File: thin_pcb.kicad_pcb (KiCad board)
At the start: 2 copper layers, 95.2 x 95.2 mm, 185 parts, among them J01 Conn_01x02, J02 Conn_01x02, J04 Conn_01x02, J06 Conn_01x02, J07 Conn_01x02, J08 Conn_01x02, J1 USB_B_Micro, J11 Conn_01x03, J12 Conn_01x03, J13 Conn_01x03, J14 Conn_01x03, J15 Conn_01x03, J16 Conn_01x03, J17 Conn_01x03, J18 Conn_01x03, J2 AudioJack4_Ground, J21 Conn_01x07, J22 Conn_01x07, J23 Conn_01x07, J24 Conn_01x07, J25 Conn_01x07, J26 Conn_01x07, J27 Conn_01x07, J28 Conn_01x07, J3 AudioJack4_Ground, J31 Conn_01x07, J32 Conn_01x07, J33 Conn_01x07, J34 Conn_01x07, J35 Conn_01x07, J36 Conn_01x07, J37 Conn_01x07, J38 Conn_01x07, J4 Conn_01x06, J41 Conn_01x04, J42 Conn_01x04, J43 Conn_01x04, J44 Conn_01x04, J45 Conn_01x04, J46 Conn_01x04, J47 Conn_01x04, J48 Conn_01x04, J5 Conn_01x06, J51 Conn_01x01, J52 Conn_01x01, J53 Conn_01x01, J54 Conn_01x01, J55 Conn_01x01, J56 Conn_01x01, J57 Conn_01x01, J58 Conn_01x01, J6 Conn_02x02, J7 Conn_01x02, SW11 SW_Push, SW12 SW_Push, SW13 SW_Push, SW14 SW_Push, SW15 SW_Push, SW21 SW_Push, SW22 SW_Push, SW23 SW_Push, SW24 SW_Push, SW25 SW_Push, SW252 SW_Push, SW31 SW_Push, SW32 SW_Push, SW33 SW_Push, SW34 SW_Push, SW35 SW_Push, SW41 SW_Push, SW42 SW_Push, SW422 SW_Push, SW43 SW_Push, SW44 SW_Push, SW45 SW_Push, SW452 SW_Push, SW51 SW_Push, SW52 SW_Push, SW522 SW_Push, SW53 SW_Push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

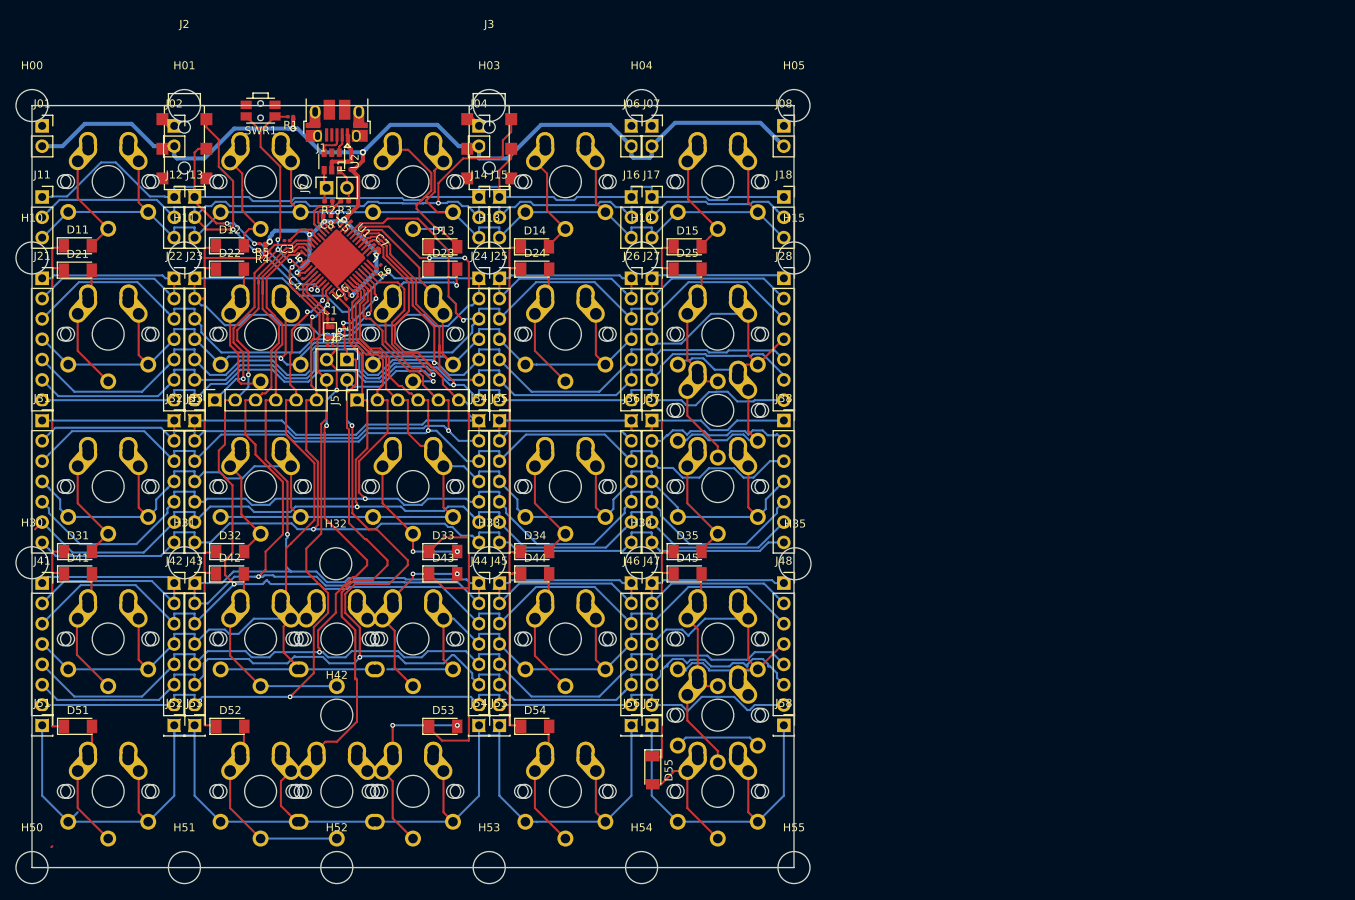
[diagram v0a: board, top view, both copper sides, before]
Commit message: hide unwanted labels
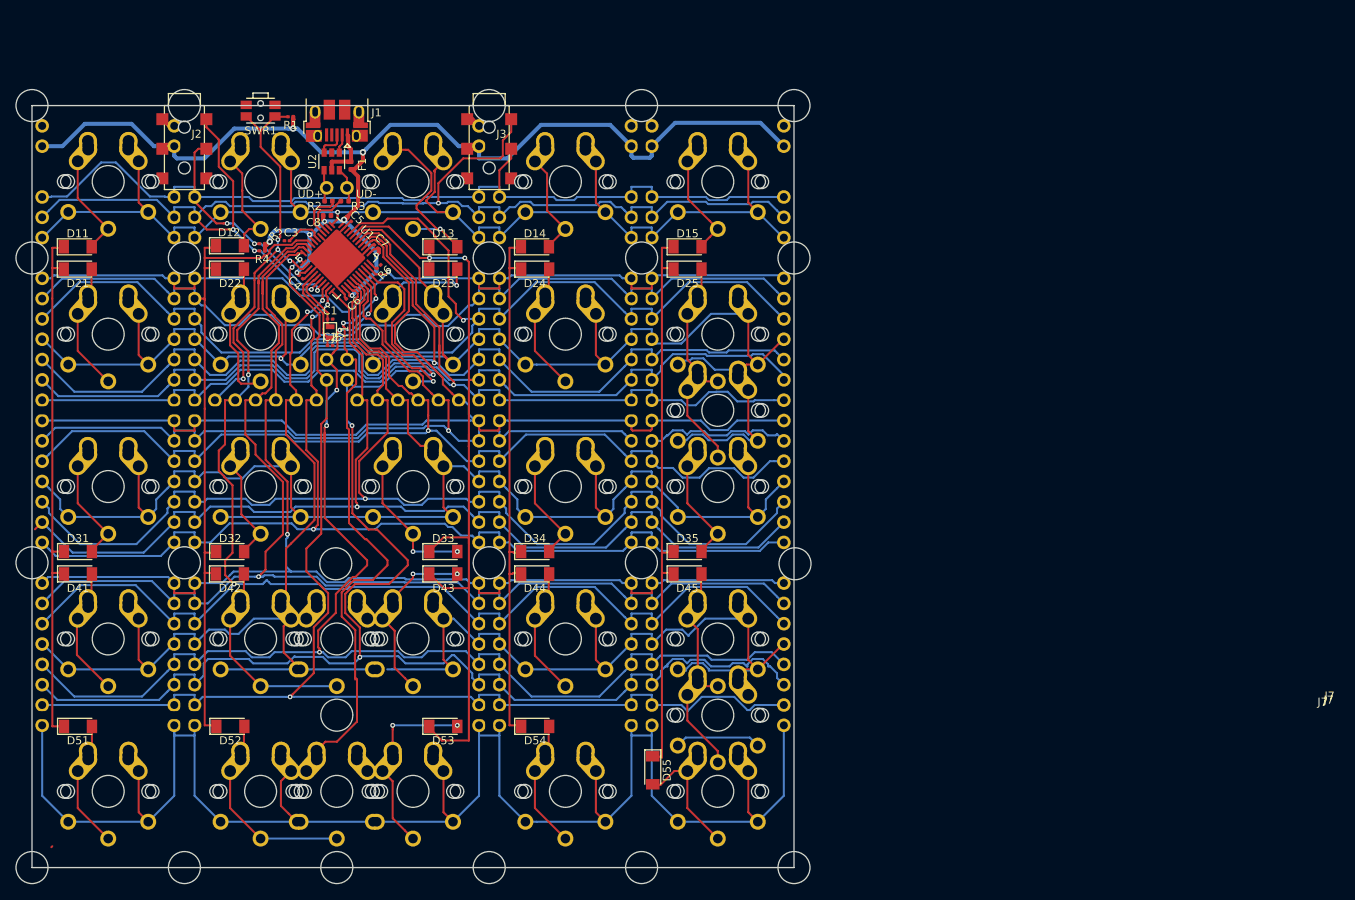
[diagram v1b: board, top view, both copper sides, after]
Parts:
- added ?: , , F.Cu at (86.7, 70.2)
- added ?: , , F.Cu at (86.0, 70.5)
- added ?: , , F.Cu at (86.9, 69.7)
- J01, J02, J04, J06, J07, J08, J7: footprint Connector_PinSocket_2.54mm:PinSocket_1x02_P2.54mm_Vertical -> lib:PinSocket_1x02_P2.54mm_Vertical
- J11, J12, J13, J14, J15, J16, J17, J18: footprint Connector_PinSocket_2.54mm:PinSocket_1x03_P2.54mm_Vertical -> lib:PinSocket_1x03_P2.54mm_Vertical
- J21, J22, J23, J24, J25, J26, J27, J28, J31, J32, J33, J34, J35, J36, J37, J38, J41, J42, J43, J44, J45, J46, J47, J48: footprint Connector_PinSocket_2.54mm:PinSocket_1x07_P2.54mm_Vertical -> lib:PinSocket_1x07_P2.54mm_Vertical
- J4, J5: footprint Connector_PinSocket_2.54mm:PinSocket_1x06_P2.54mm_Vertical -> lib:PinSocket_1x06_P2.54mm_Vertical
- J51, J52, J53, J54, J55, J56, J57, J58: footprint Connector_PinSocket_2.54mm:PinSocket_1x01_P2.54mm_Vertical -> lib:PinSocket_1x01_P2.54mm_Vertical
- J6: footprint Connector_PinSocket_2.54mm:PinSocket_2x02_P2.54mm_Vertical -> lib:PinSocket_2x02_P2.54mm_Vertical
- moved D21 0.13 mm to (57.1, 79.5)
- moved D11 0.13 mm to (57.1, 76.7)
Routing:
- net B6: track 286.6 -> 284.9 mm
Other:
- board text added: "UD+"
- board text added: "UD-"

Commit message: pin labels
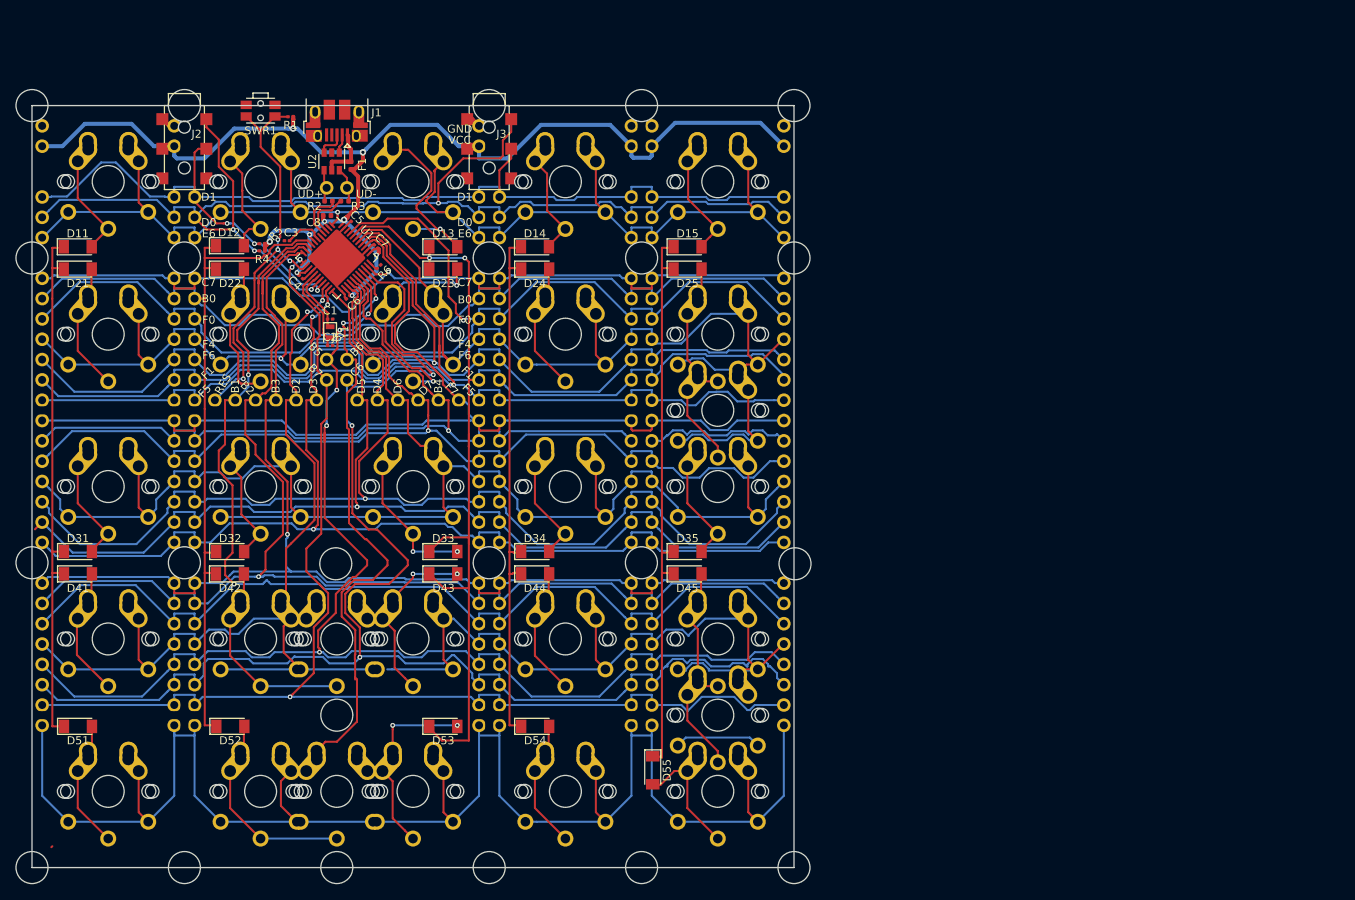
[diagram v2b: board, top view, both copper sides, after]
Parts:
- added ? (x2): , , F.Cu at (105.4, 81.9)
- added ?: , , F.Cu at (105.9, 75.6)
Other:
- board text added: "B0"
- board text added: "B1"
- board text added: "B2"
- board text added: "B3"
- board text added: "B4"
- board text added: "B5"
- board text added: "B6"
- board text added: "B7"
- board text added: "C6"
- board text added: "C7"
- board text added: "D0"
- board text added: "D1"
- board text added: "D2"
- board text added: "D3"
- board text added: "D4"
- board text added: "D5"
- board text added: "D6"
- board text added: "D7"
- board text added: "E6"
- board text added: "F0"
- board text added: "F1"
- board text added: "F4"
- board text added: "F5"
- board text added: "F6"
- board text added: "F7"
- board text added: "GND"
- board text added: "RES"
- board text added: "VCC"
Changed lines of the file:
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@@
   (general
     (thickness 1.6)
-    (drawings 6)
+    (drawings 44)
     (tracks 2140)
     (zones 0)
-    (modules 188)
+    (modules 191)
     (nets 69)
   )
@@
   )
   (module "" (layer F.Cu)
+    (at 105.41 81.915)
+    (fp_text reference "" (at 127.635 64.135) (layer F.SilkS)
+      (effects (font (size 1.27 1.27) (thickness 0.15)))
+    )
+    (fp_text value "" (at 127.635 64.135) (layer F.SilkS)
+      (effects (font (size 1.27 1.27) (thickness 0.15)))
+    )
+    (fp_text user J7 (at 84.836 45.974) (layer F.SilkS) hide
+      (effects (font (size 1 1) (thickness 0.15)))
+    )
+  )
+  (module "" (layer F.Cu)
+    (at 105.918 75.565)
+    (fp_text reference "" (at 127.635 64.135) (layer F.SilkS)
+      (effects (font (size 1.27 1.27) (thickness 0.15)))
+    )
+    (fp_text value "" (at 127.635 64.135) (layer F.SilkS)
+      (effects (font (size 1.27 1.27) (thickness 0.15)))
+    )
+    (fp_text user J7 (at 84.328 54.61) (layer F.SilkS) hide
+      (effects (font (size 1 1) (thickness 0.15)))
+    )
+  )
+  (module "" (layer F.Cu)
+    (at 105.41 81.915)
+    (fp_text reference "" (at 127.635 64.135) (layer F.SilkS)
+      (effects (font (size 1.27 1.27) (thickness 0.15)))
+    )
+    (fp_text value "" (at 127.635 64.135) (layer F.SilkS)
+      (effects (font (size 1.27 1.27) (thickness 0.15)))
+    )
+    (fp_text user J7 (at 85.09 43.307) (layer F.SilkS) hide
+      (effects (font (size 1 1) (thickness 0.15)))
+    )
+  )
+  (module "" (layer F.Cu)
     (at 86.741 70.231)
     (fp_text reference "" (at 127.635 64.135) (layer F.SilkS)
@@
       (effects (font (size 1.27 1.27) (thickness 0.15)))
     )
-    (fp_text user J7 (at 126.77 63.119) (layer F.SilkS)
+    (fp_text user J7 (at 103.124 65.913) (layer F.SilkS) hide
       (effects (font (size 1 1) (thickness 0.15)))
     )
@@
       (effects (font (size 1.27 1.27) (thickness 0.15)))
     )
-    (fp_text user J7 (at 126.77 63.119) (layer F.SilkS)
+    (fp_text user J7 (at 103.886 68.199) (layer F.SilkS) hide
       (effects (font (size 1 1) (thickness 0.15)))
     )
@@
       (effects (font (size 1.27 1.27) (thickness 0.15)))
     )
-    (fp_text user J7 (at 126.77 63.119) (layer F.SilkS)
+    (fp_text user J7 (at 103.251 63.246) (layer F.SilkS) hide
       (effects (font (size 1 1) (thickness 0.15)))
     )
@@
       (net 1 GND))
   )
+  (gr_text E6 (at 73.533 75.057) (layer F.SilkS)
+    (effects (font (size 1 1) (thickness 0.15)))
+  )
+  (gr_text D0 (at 73.533 73.66) (layer F.SilkS)
+    (effects (font (size 1 1) (thickness 0.15)))
+  )
+  (gr_text D1 (at 73.533 70.485) (layer F.SilkS)
+    (effects (font (size 1 1) (thickness 0.15)))
+  )
+  (gr_text C7 (at 73.533 81.153) (layer F.SilkS)
+    (effects (font (size 1 1) (thickness 0.15)))
+  )
+  (gr_text B0 (at 73.533 83.185) (layer F.SilkS)
+    (effects (font (size 1 1) (thickness 0.15)))
+  )
+  (gr_text F0 (at 73.533 85.852) (layer F.SilkS)
+    (effects (font (size 1 1) (thickness 0.15)))
+  )
+  (gr_text F4 (at 73.533 88.9) (layer F.SilkS)
+    (effects (font (size 1 1) (thickness 0.15)))
+  )
+  (gr_text F6 (at 73.533 90.297) (layer F.SilkS)
+    (effects (font (size 1 1) (thickness 0.15)))
+  )
+  (gr_text F1 (at 73.406 92.456 45) (layer F.SilkS)
+    (effects (font (size 1 1) (thickness 0.15)))
+  )
+  (gr_text F5 (at 73.025 94.742 45) (layer F.SilkS)
+    (effects (font (size 1 1) (thickness 0.15)))
+  )
+  (gr_text RES (at 75.311 93.853 60) (layer F.SilkS)
+    (effects (font (size 1 1) (thickness 0.15)))
+  )
+  (gr_text B1 (at 76.835 94.107 90) (layer F.SilkS)
+    (effects (font (size 1 1) (thickness 0.15)))
+  )
+  (gr_text B2 (at 78.359 94.361 315) (layer F.SilkS)
+    (effects (font (size 1 1) (thickness 0.15)))
+  )
+  (gr_text B3 (at 81.915 94.107 90) (layer F.SilkS)
+    (effects (font (size 1 1) (thickness 0.15)))
+  )
+  (gr_text D2 (at 84.455 94.107 90) (layer F.SilkS)
+    (effects (font (size 1 1) (thickness 0.15)))
+  )
+  (gr_text D3 (at 86.614 94.107 90) (layer F.SilkS)
+    (effects (font (size 1 1) (thickness 0.15)))
+  )
+  (gr_text B7 (at 86.868 92.202 315) (layer F.SilkS)
+    (effects (font (size 1 1) (thickness 0.15)))
+  )
+  (gr_text B5 (at 86.868 89.535 315) (layer F.SilkS)
+    (effects (font (size 1 1) (thickness 0.15)))
+  )
+  (gr_text B6 (at 92.075 89.535 45) (layer F.SilkS)
+    (effects (font (size 1 1) (thickness 0.15)))
+  )
+  (gr_text C6 (at 92.075 92.075 45) (layer F.SilkS)
+    (effects (font (size 1 1) (thickness 0.15)))
+  )
+  (gr_text D5 (at 92.583 94.107 90) (layer F.SilkS)
+    (effects (font (size 1 1) (thickness 0.15)))
+  )
+  (gr_text D4 (at 94.615 94.107 90) (layer F.SilkS)
+    (effects (font (size 1 1) (thickness 0.15)))
+  )
+  (gr_text D6 (at 97.155 94.107 90) (layer F.SilkS)
+    (effects (font (size 1 1) (thickness 0.15)))
+  )
+  (gr_text D7 (at 100.711 94.361 45) (layer F.SilkS)
+    (effects (font (size 1 1) (thickness 0.15)))
+  )
+  (gr_text B4 (at 102.235 94.107 90) (layer F.SilkS)
+    (effects (font (size 1 1) (thickness 0.15)))
+  )
+  (gr_text F7 (at 103.886 94.488 315) (layer F.SilkS)
+    (effects (font (size 1 1) (thickness 0.15)))
+  )
+  (gr_text F5 (at 106.045 94.615 315) (layer F.SilkS)
+    (effects (font (size 1 1) (thickness 0.15)))
+  )
+  (gr_text F1 (at 105.918 92.456 315) (layer F.SilkS)
+    (effects (font (size 1 1) (thickness 0.15)))
+  )
+  (gr_text F6 (at 105.537 90.297) (layer F.SilkS)
+    (effects (font (size 1 1) (thickness 0.15)))
+  )
+  (gr_text F4 (at 105.537 88.9) (layer F.SilkS)
+    (effects (font (size 1 1) (thickness 0.15)))
+  )
+  (gr_text F0 (at 105.537 85.852) (layer F.SilkS)
+    (effects (font (size 1 1) (thickness 0.15)))
+  )
+  (gr_text B0 (at 105.537 83.312) (layer F.SilkS)
+    (effects (font (size 1 1) (thickness 0.15)))
+  )
+  (gr_text C7 (at 105.537 81.153) (layer F.SilkS)
+    (effects (font (size 1 1) (thickness 0.15)))
+  )
+  (gr_text E6 (at 105.537 75.057) (layer F.SilkS)
+    (effects (font (size 1 1) (thickness 0.15)))
+  )
+  (gr_text D0 (at 105.537 73.66) (layer F.SilkS)
+    (effects (font (size 1 1) (thickness 0.15)))
+  )
+  (gr_text D1 (at 105.537 70.485) (layer F.SilkS)
+    (effects (font (size 1 1) (thickness 0.15)))
+  )
+  (gr_text VCC (at 104.902 63.373) (layer F.SilkS)
+    (effects (font (size 1 1) (thickness 0.15)))
+  )
+  (gr_text GND (at 104.902 61.976) (layer F.SilkS)
+    (effects (font (size 1 1) (thickness 0.15)))
+  )
   (gr_text UD+ (at 86.233 70.104) (layer F.SilkS)

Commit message: 3d pics
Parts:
- removed the ? at (105.4, 81.9) (x2)
- added ? (x2): , , F.Cu at (105.4, 81.9)
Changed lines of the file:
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@@
     (add_net VCC)
   )
+  (module lib:PinSocket_2x02_P2.54mm_Vertical (layer F.Cu)
+    (at 90.805 90.805)
+    (descr "Through hole straight socket strip, 2x02, 2.54mm pitch, double cols (from Kicad 4.0.7), script generated")
+    (tags "Through hole socket strip THT 2x02 2.54mm double row")
+    (fp_text reference J6 (at -1.27 -2.77) (layer F.SilkS)
+      (effects (font (size 1 1) (thickness 0.15)))
+    )
+    (fp_text value Conn_02x02 (at -1.27 5.31) (layer F.Fab)
+      (effects (font (size 1 1) (thickness 0.15)))
+    )
+    (fp_line (start -3.81 -1.27) (end 0.27 -1.27) (layer F.Fab) (width 0.1))
+    (fp_line (start 0.27 -1.27) (end 1.27 -0.27) (layer F.Fab) (width 0.1))
+    (fp_line (start 1.27 -0.27) (end 1.27 3.81) (layer F.Fab) (width 0.1))
+    (fp_line (start 1.27 3.81) (end -3.81 3.81) (layer F.Fab) (width 0.1))
+    (fp_line (start -3.81 3.81) (end -3.81 -1.27) (layer F.Fab) (width 0.1))
+    (fp_line (start -4.34 -1.8) (end 1.76 -1.8) (layer F.CrtYd) (width 0.05))
+    (fp_line (start 1.76 -1.8) (end 1.76 4.3) (layer F.CrtYd) (width 0.05))
+    (fp_line (start 1.76 4.3) (end -4.34 4.3) (layer F.CrtYd) (width 0.05))
+    (fp_line (start -4.34 4.3) (end -4.34 -1.8) (layer F.CrtYd) (width 0.05))
+    (fp_text user %R (at -1.27 1.27 90) (layer F.Fab) hide
+      (effects (font (size 1 1) (thickness 0.15)))
+    )
+    (pad 1 thru_hole oval (at 0 0) (size 1.7 1.7) (drill 1) (layers *.Cu *.Mask)
+      (net 45 B6))
+    (pad 2 thru_hole oval (at -2.54 0) (size 1.7 1.7) (drill 1) (layers *.Cu *.Mask)
+      (net 44 B5))
+    (pad 3 thru_hole oval (at 0 2.54) (size 1.7 1.7) (drill 1) (layers *.Cu *.Mask)
+      (net 47 C6))
+    (pad 4 thru_hole oval (at -2.54 2.54) (size 1.7 1.7) (drill 1) (layers *.Cu *.Mask)
+      (net 46 B7))
+  )
   (module "" (layer F.Cu)
     (at 105.41 81.915)
@@
       (net 5 VCC))
   )
-  (module lib:PinSocket_2x02_P2.54mm_Vertical (layer F.Cu)
-    (at 90.805 90.805)
-    (descr "Through hole straight socket strip, 2x02, 2.54mm pitch, double cols (from Kicad 4.0.7), script generated")
-    (tags "Through hole socket strip THT 2x02 2.54mm double row")
-    (fp_text reference J6 (at -1.27 -2.77) (layer F.SilkS)
-      (effects (font (size 1 1) (thickness 0.15)))
-    )
-    (fp_text value Conn_02x02 (at -1.27 5.31) (layer F.Fab)
-      (effects (font (size 1 1) (thickness 0.15)))
-    )
-    (fp_text user %R (at -1.27 1.27 90) (layer F.Fab) hide
-      (effects (font (size 1 1) (thickness 0.15)))
-    )
-    (fp_line (start -4.34 4.3) (end -4.34 -1.8) (layer F.CrtYd) (width 0.05))
-    (fp_line (start 1.76 4.3) (end -4.34 4.3) (layer F.CrtYd) (width 0.05))
-    (fp_line (start 1.76 -1.8) (end 1.76 4.3) (layer F.CrtYd) (width 0.05))
-    (fp_line (start -4.34 -1.8) (end 1.76 -1.8) (layer F.CrtYd) (width 0.05))
-    (fp_line (start -3.81 3.81) (end -3.81 -1.27) (layer F.Fab) (width 0.1))
-    (fp_line (start 1.27 3.81) (end -3.81 3.81) (layer F.Fab) (width 0.1))
-    (fp_line (start 1.27 -0.27) (end 1.27 3.81) (layer F.Fab) (width 0.1))
-    (fp_line (start 0.27 -1.27) (end 1.27 -0.27) (layer F.Fab) (width 0.1))
-    (fp_line (start -3.81 -1.27) (end 0.27 -1.27) (layer F.Fab) (width 0.1))
-    (pad 4 thru_hole oval (at -2.54 2.54) (size 1.7 1.7) (drill 1) (layers *.Cu *.Mask)
-      (net 46 B7))
-    (pad 3 thru_hole oval (at 0 2.54) (size 1.7 1.7) (drill 1) (layers *.Cu *.Mask)
-      (net 47 C6))
-    (pad 2 thru_hole oval (at -2.54 0) (size 1.7 1.7) (drill 1) (layers *.Cu *.Mask)
-      (net 44 B5))
-    (pad 1 thru_hole oval (at 0 0) (size 1.7 1.7) (drill 1) (layers *.Cu *.Mask)
-      (net 45 B6))
-    (model ${KISYS3DMOD}/Connector_PinSocket_2.54mm.3dshapes/PinSocket_2x02_P2.54mm_Vertical.wrl
-      (at (xyz 0 0 0))
-      (scale (xyz 1 1 1))
-      (rotate (xyz 0 0 0))
-    )
-  )
   (module lib:PinSocket_1x02_P2.54mm_Vertical (layer F.Cu)
